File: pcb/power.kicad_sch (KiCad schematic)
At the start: 19 parts, among them J3 XT30PW-M, J4 Screw_Terminal_01x02, Q2 NTR4003N, U3 TPS561246DRLR, U5 ZXCT180B3W5

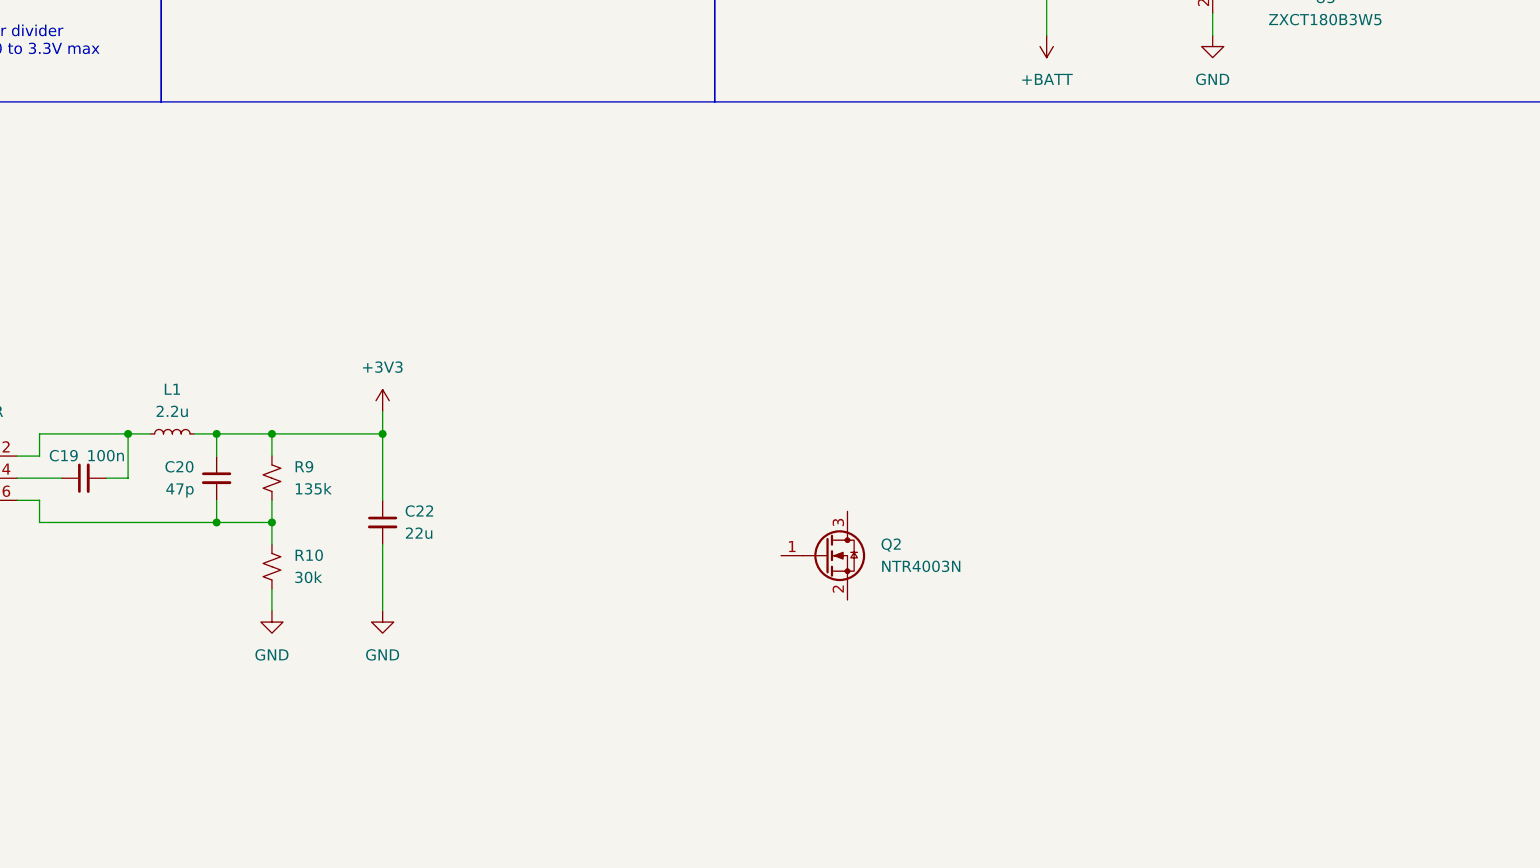
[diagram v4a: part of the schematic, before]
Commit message: Draw battery switch PMOS driver
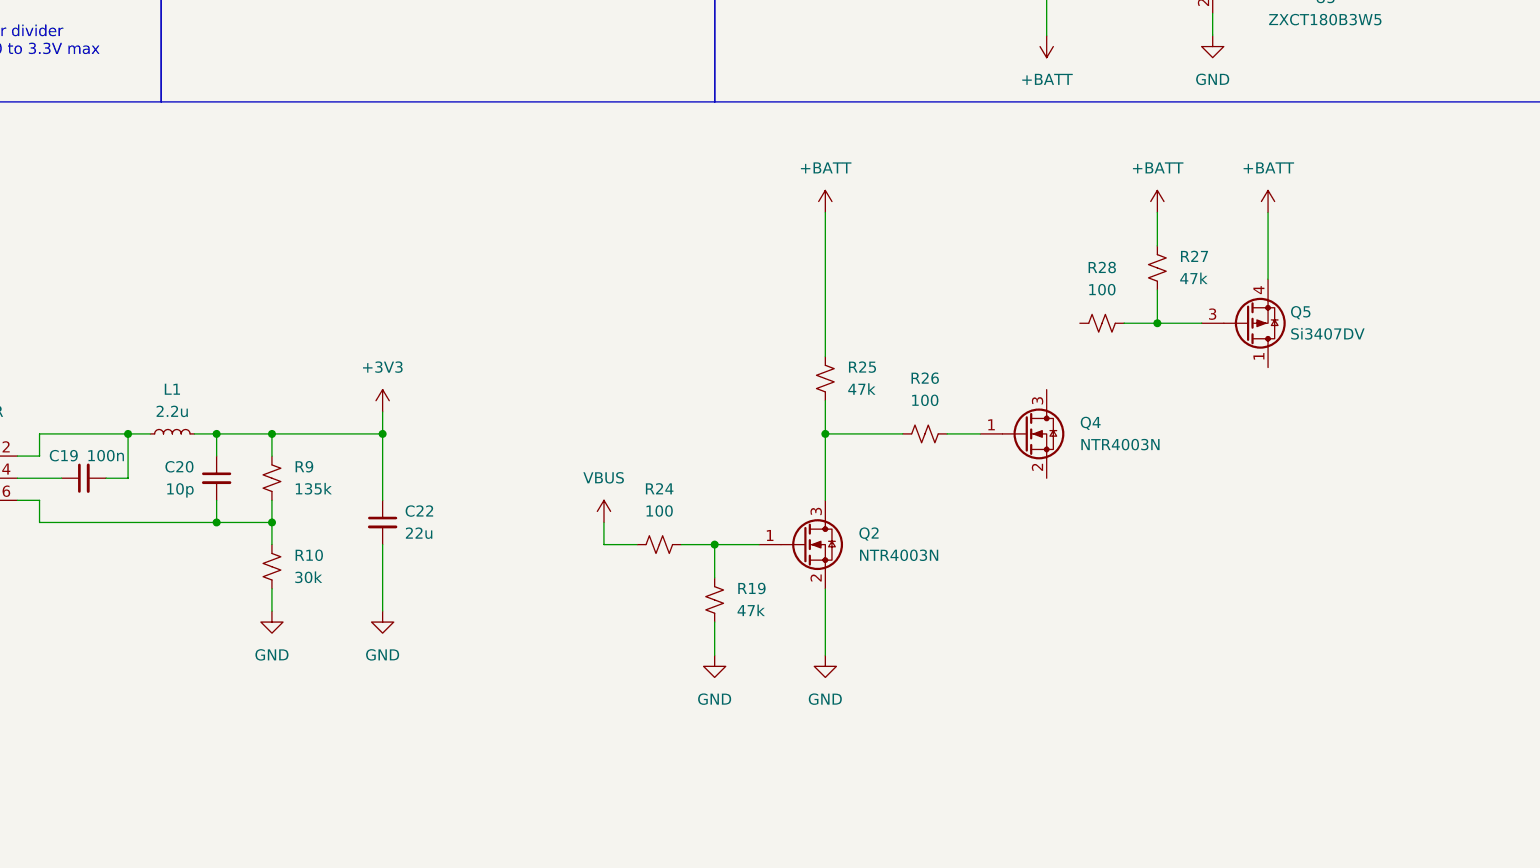
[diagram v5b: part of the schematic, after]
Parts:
- added Q4: NTR4003N, Package_TO_SOT_SMD:SOT-23-3, symbol Transistor_FET:Q_NMOS_GSD
- added Q5: Si3407DV, Package_SO:TSOP-6_1.65x3.05mm_P0.95mm, symbol Vishay_FET:Si3407DV
- added R19, R25, R27: 47k, symbol Device:R_Small_US
- added R24, R26, R28: 100, symbol Device:R_Small_US
- C20: value 47p -> 10p
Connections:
- net +BATT: now also Q5.4 (S), R25.1, R27.1
- net GND: now also Q2.2 (S), R19.2
- net at Q2.1 (G): now also R19.1, R24.2
- net at Q2.3 (D): now also R25.2, R26.1
- new net: Q4.1 (G), R26.2
- new net: Q5.3 (G), R27.2, R28.2
- new net: Q5.1 (D), Q5.2 (D), Q5.5 (D), Q5.6 (D)
- new net VBUS: R24.1
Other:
- moved on the sheet: Q2

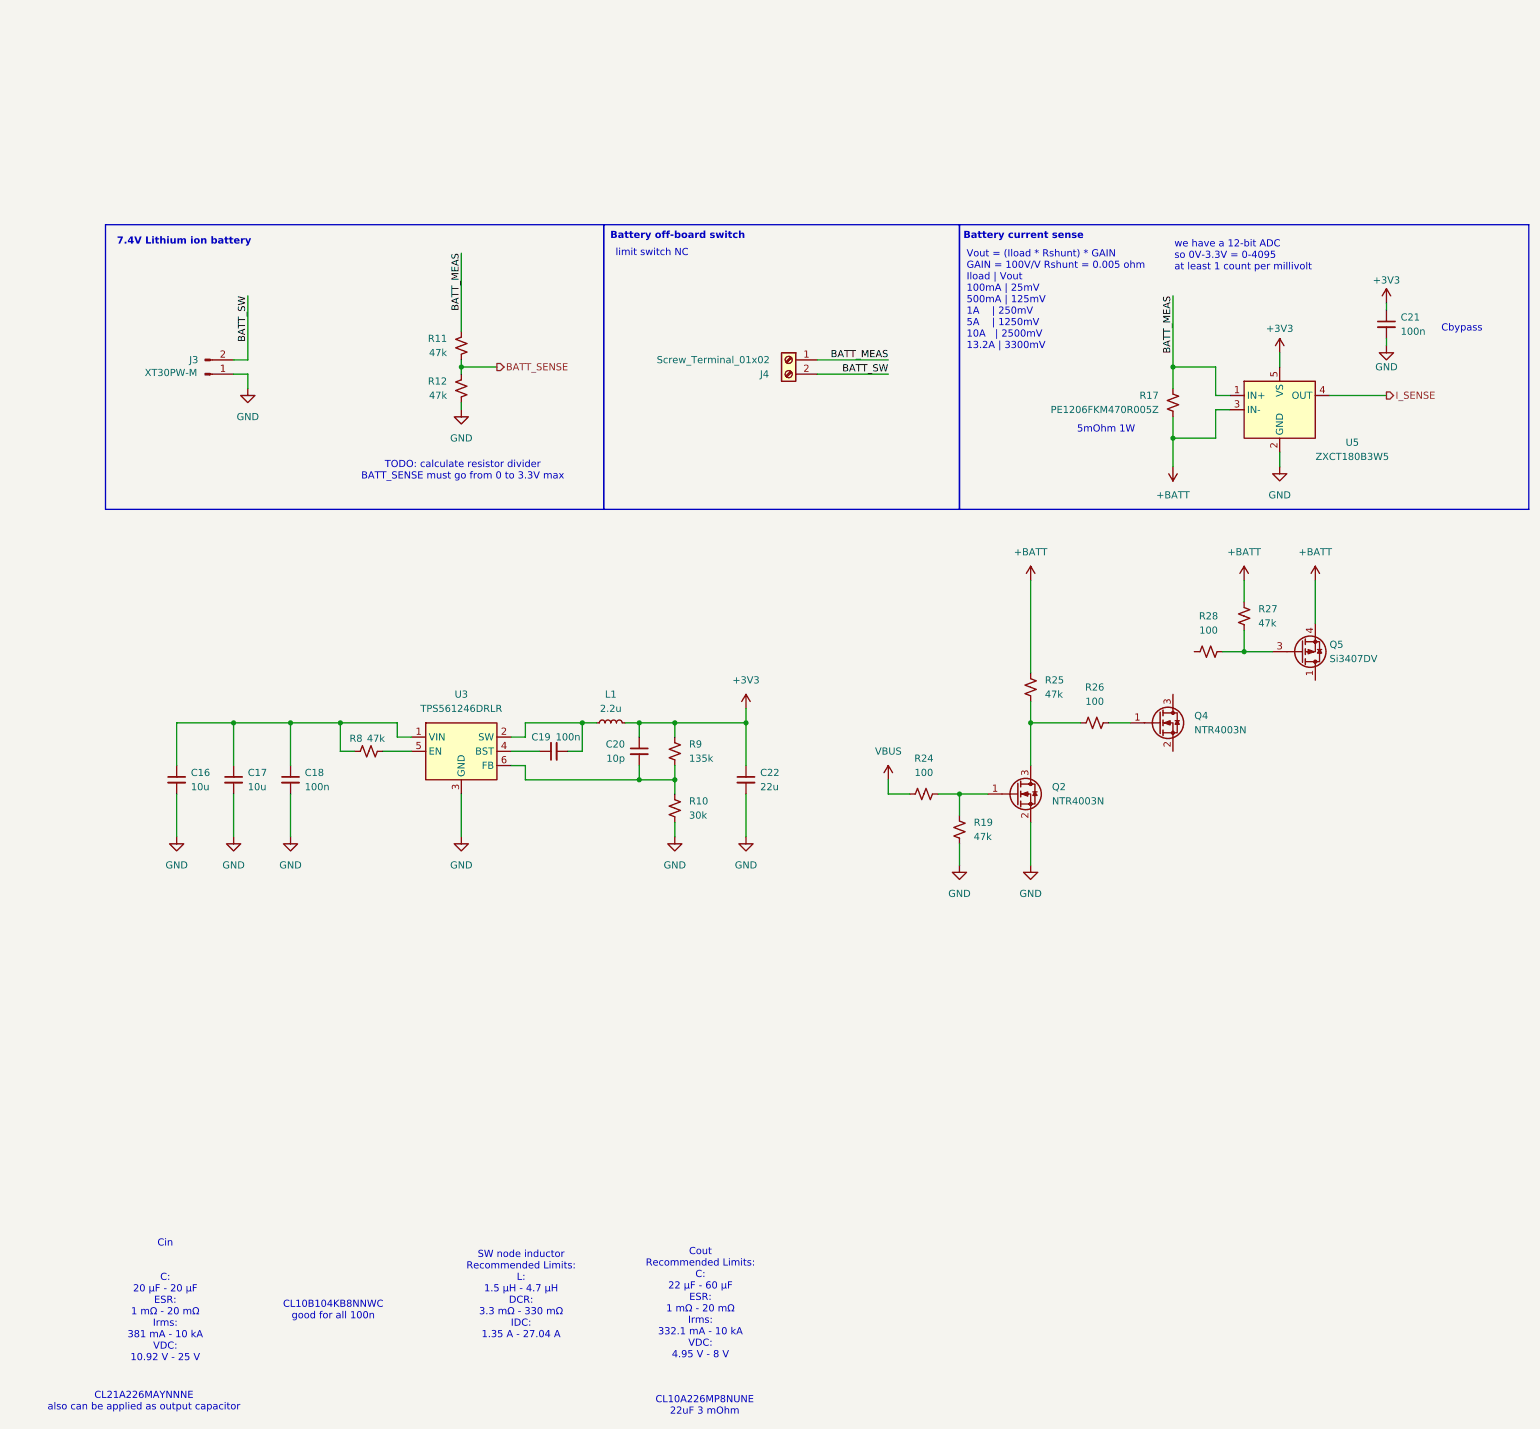
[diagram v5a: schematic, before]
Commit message: Finish and simplify power schematics
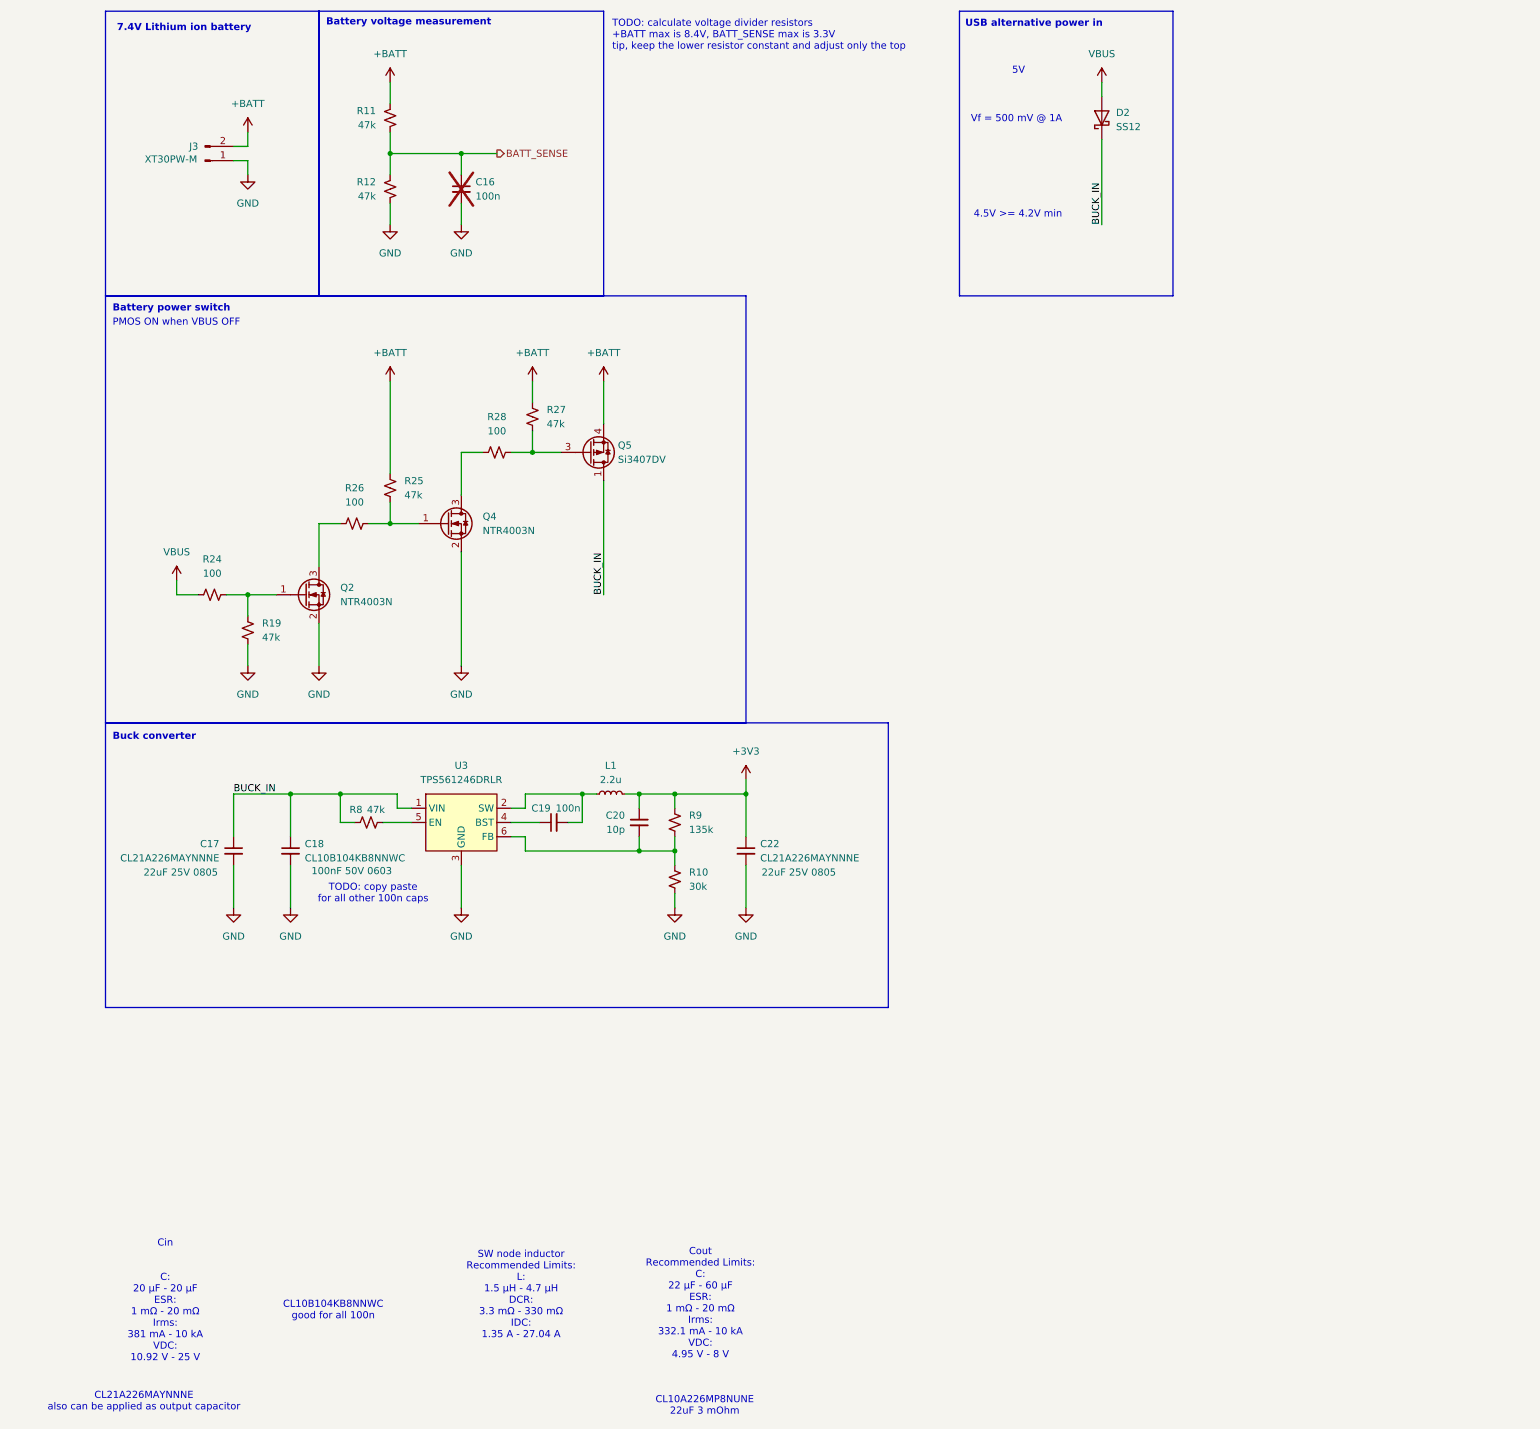
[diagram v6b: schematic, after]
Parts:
- removed C21: 100n, Capacitor_SMD:C_0603_1608Metric, symbol Device:C_Small
- removed J4: Screw_Terminal_01x02, Wurth_ScrewTerminal_691137710002:Wurth_ScrewTerminal_691137710002, symbol Connector:Screw_Terminal_01x02
- removed R17: PE1206FKM470R005Z, Resistor_SMD:R_1206_3216Metric, symbol Device:R_Small_US
- removed U5: ZXCT180B3W5, Package_TO_SOT_SMD:SOT-23-5, symbol DI_ZXCT180:ZXCT180B2
- added D2: SS12, Diode_SMD:D_SMA, symbol Diode:SS12
- C16: value 10u -> 100n; now not fitted
- C17: value 10u -> CL21A226MAYNNNE
- C18: value 100n -> CL10B104KB8NNWC; footprint (none) -> Capacitor_SMD:C_0603_1608Metric
- C22: value 22u -> CL21A226MAYNNNE
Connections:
- net BATT_MEAS is gone; now on net +BATT: R11.1
- net BATT_SW is gone; now on net +BATT: J3.2 (Pin_2)
- net BATT_SENSE: now also C16.1
- net GND: now also Q4.2 (S)
- net VBUS: now also D2.2 (A)
- net BUCK_IN: now reaches C17.1, C18.1, R8.1, U3.1 (VIN)
- net BUCK_IN: now also Q5.1 (D), Q5.2 (D), Q5.5 (D), Q5.6 (D), D2.1 (K); no longer C16.1
- net at Q4.1 (G), R26.2: now also R25.2
- net at Q4.3 (D): now also R28.1
- net at Q2.3 (D), R26.1: no longer R25.2
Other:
- note added: "4.5V >= 4.2V min"
- note added: "5V"
- note added: "Battery power switch"
- note added: "Battery voltage measurement"
- note added: "Buck converter"
- note added: "PMOS ON when VBUS OFF"
- note added: "TODO: calculate voltage divider resistors +BATT max is 8.4V, BATT_SENSE max is 3.3V tip, keep the lower resistor constant and adjust only the top"
- note added: "TODO: copy paste for all other 100n caps"
- note added: "USB alternative power in"
- note added: "Vf = 500 mV @ 1A"
- note removed: "5mOhm 1W"
- note removed: "Battery current sense"
- note removed: "Battery off-board switch"
- note removed: "Cbypass"
- note removed: "TODO: calculate resistor divider BATT_SENSE must go from 0 to 3.3V max"
- note removed: "Vout = (Iload * Rshunt) * GAIN GAIN = 100V/V Rshunt = 0.005 ohm Iload | Vout 100mA | 25mV 500mA | 125mV 1A | 250mV 5A | 1250mV 10A | 2500mV 13.2A | 3300mV"
- note removed: "limit switch NC"
- note removed: "we have a 12-bit ADC so 0V-3.3V = 0-4095 at least 1 count per millivolt"
- moved on the sheet: C17, C18, C19, C20, J3, L1, Q2, Q4, Q5, R10, R11, R12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
